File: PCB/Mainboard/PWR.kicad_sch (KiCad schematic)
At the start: 0 parts

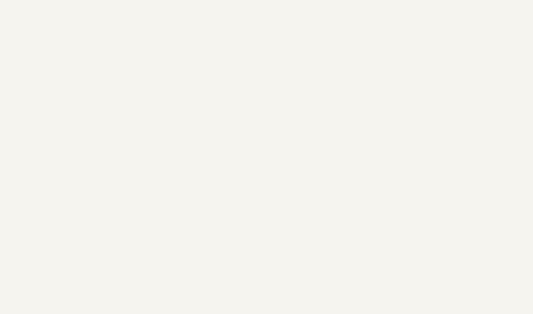
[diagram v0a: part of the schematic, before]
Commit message: Added setup, read and get Command
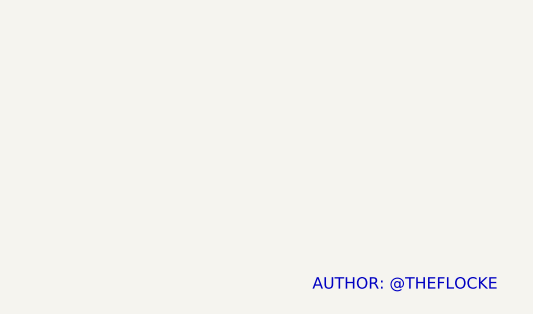
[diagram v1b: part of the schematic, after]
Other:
- note added: "AUTHOR: @THEFLOCKE"
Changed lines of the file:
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@@
 	(generator_version "9.0")
 	(paper "A4")
+	(text "AUTHOR: @THEFLOCKE"
+		(exclude_from_sim no)
+		(at 249.936 196.596 0)
+		(effects
+			(font
+				(face "KiCad Font")
+				(size 1.27 1.27)
+				(color 194 0 194 1)
+			)
+		)
+	)
 	(sheet
 		(at 25.4 25.4)
